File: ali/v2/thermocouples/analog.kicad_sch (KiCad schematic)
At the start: 51 parts, among them U5 ADS124S08

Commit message: mfw tcs
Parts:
- removed C30, C40: 1nF, APRL_Passive:C_0603, symbol Device:C_Small
- removed C32: 10nF, APRL_Passive:C_0603, symbol Device:C_Small
- removed C36: 22uF, APRL_Passive:C_0805, symbol Device:C_Small
- removed C48: 100nF, APRL_Passive:C_0603, symbol Device:C_Small
- removed R21: 10R, APRL_Passive:R_0603, symbol Device:R_Small_US
- removed R24: 100k, APRL_Passive:R_0603, symbol Device:R_Small_US
- added C33, C53, C54: 1nF, APRL_Passive:C_0603, symbol Device:C_Small
- added C45: 10nF, APRL_Passive:C_0603, symbol Device:C_Small
- added J10, J11, J12, J13, J14, J9: Conn_01x02, APRL_Connector:PCC-SMP-V-K, symbol Connector_Generic:Conn_01x02
- added R19, R34, R35, R36, R37, R42, R43: 10M, APRL_Passive:R_0603, symbol Device:R_Small_US
- added R22, R33, R38, R39, R40, R41: 1k, APRL_Passive:R_0603, symbol Device:R_Small_US
- C35: value 100nF -> 10nF; MPN GRM188R72A104KA35 -> GRM21B5C2E103FWAA
- C38: value 1nF -> 100nF; MPN GRM21B5C2J102FWA3 -> GRM188R72A104KA35
- C39: value 1nF -> 22uF; footprint APRL_Passive:C_0603 -> APRL_Passive:C_0805; MPN GRM21B5C2J102FWA3 -> GRM21BZ71A226ME15
- C41, C42, C49, C50: value 10nF -> 1nF; MPN GRM21B5C2E103FWAA -> GRM21B5C2J102FWA3
- C44, C51, C52: value 1nF -> 10nF; MPN GRM21B5C2J102FWA3 -> GRM21B5C2E103FWAA
- R20, R26, R27, R28, R29: value 1k -> 10M; MPN RT0603BRD071KL -> AC0603FR-0710ML
- R23: value 1k -> 10R; MPN RT0603BRD071KL -> RC0603FR-0710RL
- renumbered C29 to C32, C31 to C34, C33 to C36, C34 to C37, C37 to C40, C45 to C48, R19 to R21, R22 to R24, U5 to U6
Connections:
- net +5V: now also R20.1, R23.2, R28.1, R29.1, R19.1, R36.1, R37.1; no longer U6.30 (REFP0)
- net AIN0: now also C50.1, C52.2, R39.2; no longer C32.1, C34.2, R21.2
- net AIN1: now also C52.1, C54.2, R41.2; no longer C34.1, C40.2, R24.2
- net AIN10: now also C32.1, C34.2, R21.2; no longer C47.1, C50.2, R30.2
- net AIN11: now also C34.1, C40.2, R24.2; no longer C50.1, C52.2, R32.2
- net AIN2: now also C49.1, C51.2, R38.2; no longer C39.1, C41.2, R25.2
- net AIN3: now also C51.1, C53.2, R40.2; no longer C41.1, C43.2, R27.2
- net AIN4: now also C43.1, R31.2, C45.2; no longer C46.1, C49.2, R29.2
- net AIN5: now also C47.2, C45.1, R33.2; no longer C49.1, C51.2, R31.2
- net AIN6: now also C42.1, C44.2, R30.2; no longer R20.2
- net AIN7: now also C44.1, C46.2, R32.2; no longer C38.2, R23.2
- net AIN8: now also C35.2, C33.1, R22.2; no longer C42.2, R26.2
- net AIN9: now also C35.1, C41.2, R25.2; no longer C42.1, C44.2, R28.2
- net GND: now also C38.2, C41.1, C42.2, C43.2, C46.1, C47.1, C49.2, C50.2, R26.2, R27.2, U6.1 (AINCOM), U6.17 (CLK), C33.2, C53.1, C54.1, R34.2, R35.2, R42.2, R43.2; no longer C35.2, C38.1, C43.1, C44.1, C46.2, C47.2, C51.1, C52.1, U6.29 (REFN0)
- net at R32.1: now also D11.1 (A1), J11.2 (Pin_2), R34.1; no longer D17.1 (A1)
- net at U6.26 (AVDD): now also C38.1, C39.1, R23.1; no longer C35.1
- net at D9.1 (A1): now also R25.1, R27.1, J10.2 (Pin_2); no longer R23.1
- net at R30.1: now also D10.1 (A1), R28.2, J11.1 (Pin_1); no longer D16.1 (A1)
- net at D14.1 (A1): now also J13.1 (Pin_1), R36.2, R38.1; no longer R29.1
- net at D7.1 (A1), R24.1: now also R26.1, J9.2 (Pin_2)
- net at R31.1: now also D12.1 (A1), R29.2, J12.1 (Pin_1); no longer D15.1 (A1)
- net at D8.1 (A1): now also R20.2, J10.1 (Pin_1), R22.1; no longer R20.1
- net at D6.1 (A1), R21.1: now also J9.1 (Pin_1), R19.2
- net at D13.1 (A1): now also J12.2 (Pin_2), R33.1, R35.1; no longer R28.1
- new net: D15.1 (A1), J13.2 (Pin_2), R40.1, R42.1
- new net: D16.1 (A1), J14.1 (Pin_1), R37.2, R39.1
- new net: D17.1 (A1), J14.2 (Pin_2), R41.1, R43.1
- no-connect marks 1 -> 2
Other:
- note added: "I *think* this should bias to +2.5V but we'll probably need a lab bench PSU + high digit voltmeter to calibrate these inputs the TI example uses a whole 3458A to calibrate out the bias caused by the 10M resistor's tolerances"
- note added: "Not sure if 10M is the correct choice either"
- note added: "See SDAA150 for reference"
- moved on the sheet: D6, D7

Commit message: Small stuff
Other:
- note added: "Not sure if we should be using the LDO output instead of +5V, as there will probably be a ~50mV ripple at ~60 MHz"
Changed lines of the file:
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@@
+		)
+	)
+	(text "Not sure if we should be using the LDO output instead of +5V,\nas there will probably be a ~50mV ripple at ~60 MHz"
+		(exclude_from_sim no)
+		(at 233.172 39.878 0)
+		(effects
+			(font
+				(size 1.27 1.27)
+			)
 		)
 	)

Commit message: Minor thermocouple updates
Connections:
- net at D12.1 (A1), R29.2, R31.1: now also J11.1 (Pin_1); no longer J12.1 (Pin_1)
- net at D14.1 (A1), R36.2, R38.1: now also J10.1 (Pin_1); no longer J13.1 (Pin_1)
- net at D15.1 (A1), R40.1, R42.1: now also J10.2 (Pin_2); no longer J13.2 (Pin_2)
- net at D9.1 (A1), R25.1, R27.1: now also J13.2 (Pin_2); no longer J10.2 (Pin_2)
- net at D11.1 (A1), R32.1, R34.1: now also J12.2 (Pin_2); no longer J11.2 (Pin_2)
- net at D7.1 (A1), R24.1, R26.1: now also J14.2 (Pin_2); no longer J9.2 (Pin_2)
- net at D6.1 (A1), R19.2, R21.1: now also J14.1 (Pin_1); no longer J9.1 (Pin_1)
- net at D10.1 (A1), R28.2, R30.1: now also J12.1 (Pin_1); no longer J11.1 (Pin_1)
- net at D16.1 (A1), R37.2, R39.1: now also J9.1 (Pin_1); no longer J14.1 (Pin_1)
- net at D17.1 (A1), R41.1, R43.1: now also J9.2 (Pin_2); no longer J14.2 (Pin_2)
- net at D8.1 (A1), R20.2, R22.1: now also J13.1 (Pin_1); no longer J10.1 (Pin_1)
- net at D13.1 (A1), R33.1, R35.1: now also J11.2 (Pin_2); no longer J12.2 (Pin_2)
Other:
- moved on the sheet: C32, C33, C34, C35, C40, C41, C42, C43, C44, C45, C46, C47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

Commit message: Globally remove LCSC labels, update MPNs and IOCs, add +5V monitoring to DAQs, fix some footprints
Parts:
- C32: renamed from C50; MPN GRM21B5C2J102FWA3 -> GRM1885C1H102FA01
- C33: renamed from C49; MPN GRM21B5C2J102FWA3 -> GRM1885C1H102FA01
- C38: renamed from C52; MPN GRM21B5C2E103FWAA -> GRM1885C1H103JA01
- C39: renamed from C51; MPN GRM21B5C2E103FWAA -> GRM1885C1H103JA01
- C40: renamed from C54; MPN GRM21B5C2J102FWA3 -> GRM1885C1H102FA01
- C41: renamed from C53; MPN GRM21B5C2J102FWA3 -> GRM1885C1H102FA01
- C42: renamed from C43; MPN GRM21B5C2J102FWA3 -> GRM1885C1H102FA01
- C43: renamed from C42; MPN GRM21B5C2J102FWA3 -> GRM1885C1H102FA01
- C44: renamed from C45; MPN GRM21B5C2E103FWAA -> GRM1885C1H103JA01
- C45: renamed from C44; MPN GRM21B5C2E103FWAA -> GRM1885C1H103JA01
- C47: MPN GRM21B5C2J102FWA3 -> GRM1885C1H102FA01
- C48: renamed from C46; MPN GRM21B5C2J102FWA3 -> GRM1885C1H102FA01
- C49: renamed from C33; MPN GRM21B5C2J102FWA3 -> GRM1885C1H102FA01
- C50: renamed from C32; MPN GRM21B5C2J102FWA3 -> GRM1885C1H102FA01
- C51: renamed from C35; MPN GRM21B5C2E103FWAA -> GRM1885C1H103JA01
- C52: renamed from C34; MPN GRM21B5C2E103FWAA -> GRM1885C1H103JA01
- C53: renamed from C41; MPN GRM21B5C2J102FWA3 -> GRM1885C1H102FA01
- C54: renamed from C40; MPN GRM21B5C2J102FWA3 -> GRM1885C1H102FA01
- U6: footprint APRL_Package:QFN-32_EP_5.8x5.8_Pitch0.5mm -> APRL_Package_QFN:Texas_RHB0032M_VQFN-32-1EP_5x5mm_P0.5mm_EP2.1x2.1mm_ThermalVias
- renumbered C36 to C34, C37 to C35, C38 to C36, C39 to C37, C48 to C46, D12 to D10, D13 to D11, D10 to D12, D11 to D13, D8 to D14, D9 to D15, D6 to D16, D7 to D17, D16 to D6, D17 to D7, D14 to D8, D15 to D9, R37 to R21, R36 to R22, R39 to R24, R38 to R25, R41 to R26, R40 to R27, R43 to R28, R42 to R29, R29 to R30, R28 to R31, R31 to R32, R30 to R33, R33 to R34, R32 to R35, R35 to R36, R34 to R37, R20 to R38, R19 to R39, R22 to R40, R21 to R41, R25 to R42, R24 to R43, R27 to R44, R26 to R45

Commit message: Small documentation
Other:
- note added: "ADC"
- note added: "INPUTS"
- moved on the sheet: C32, C33, C34, C35, C36, C37, C38, C39, C40, C41, C42, C43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

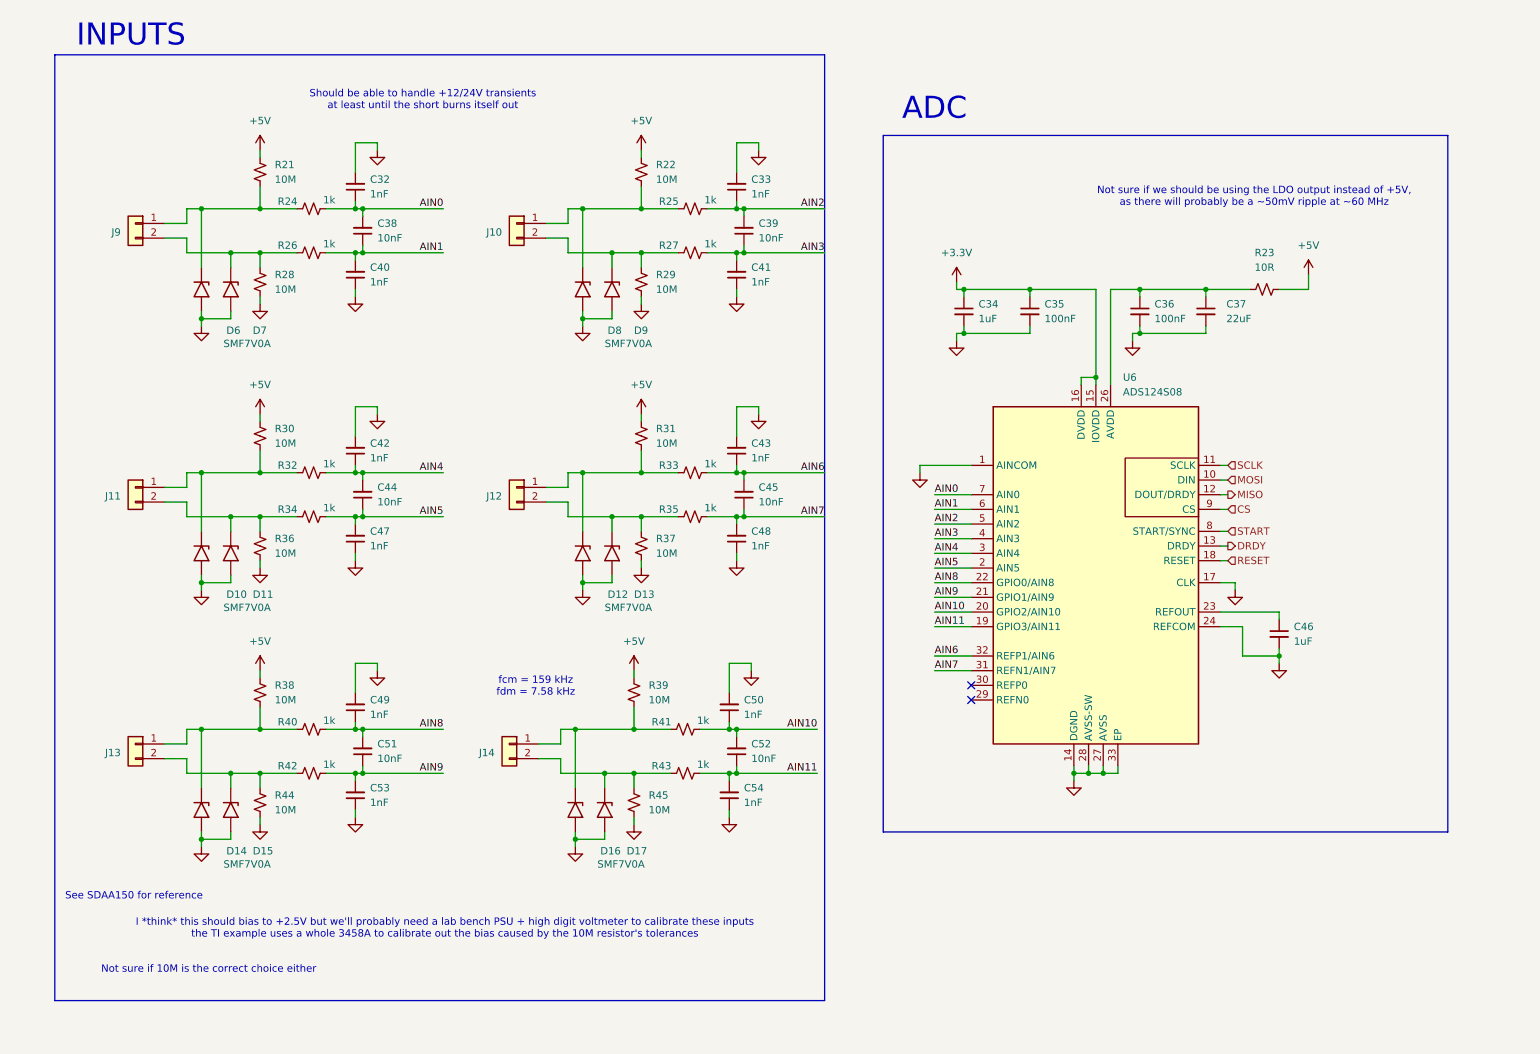
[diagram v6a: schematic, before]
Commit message: the great flatpak and kicad 10.0.6 migration
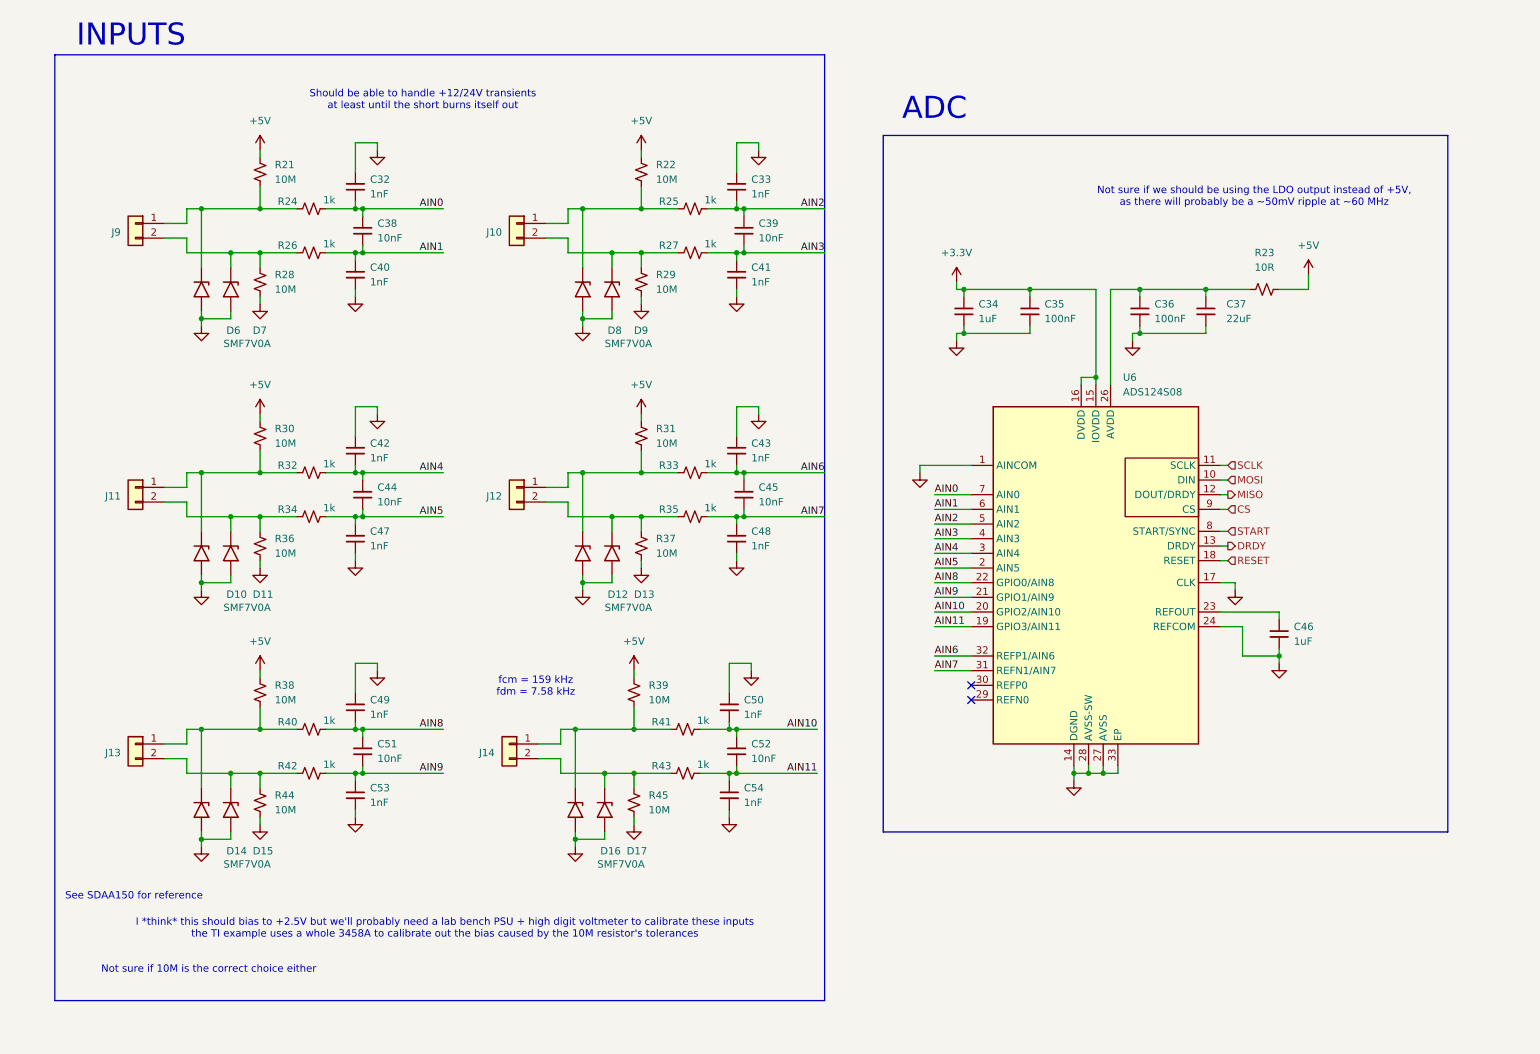
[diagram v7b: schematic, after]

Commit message: Add more commentary
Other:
- note added: "I decided that an ADS1261 is a waste on this board"
- note added: "I think we can reference this to AINCOM instead of +5V and GND but I'm not totally sure"
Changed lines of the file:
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@@
+		)
+	)
+	(text "I decided that an ADS1261 is a waste on this board"
+		(exclude_from_sim no)
+		(at 196.85 163.83 0)
+		(effects
+			(font
+				(size 1.27 1.27)
+			)
 		)
 	)
@@
 		(effects
 			(font
+				(size 1.27 1.27)
+			)
+		)
+	)
+	(text "I think we can reference this to AINCOM instead of +5V and GND but I'm not totally sure"
+		(exclude_from_sim no)
+		(at 146.304 27.432 0)
+		(effects
+			(font
